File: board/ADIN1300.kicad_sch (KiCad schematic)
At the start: 38 parts, among them U1 ADIN1300BCPZ, U2 TLV71209_SOT23-5, Y1 Crystal_GND24_Small

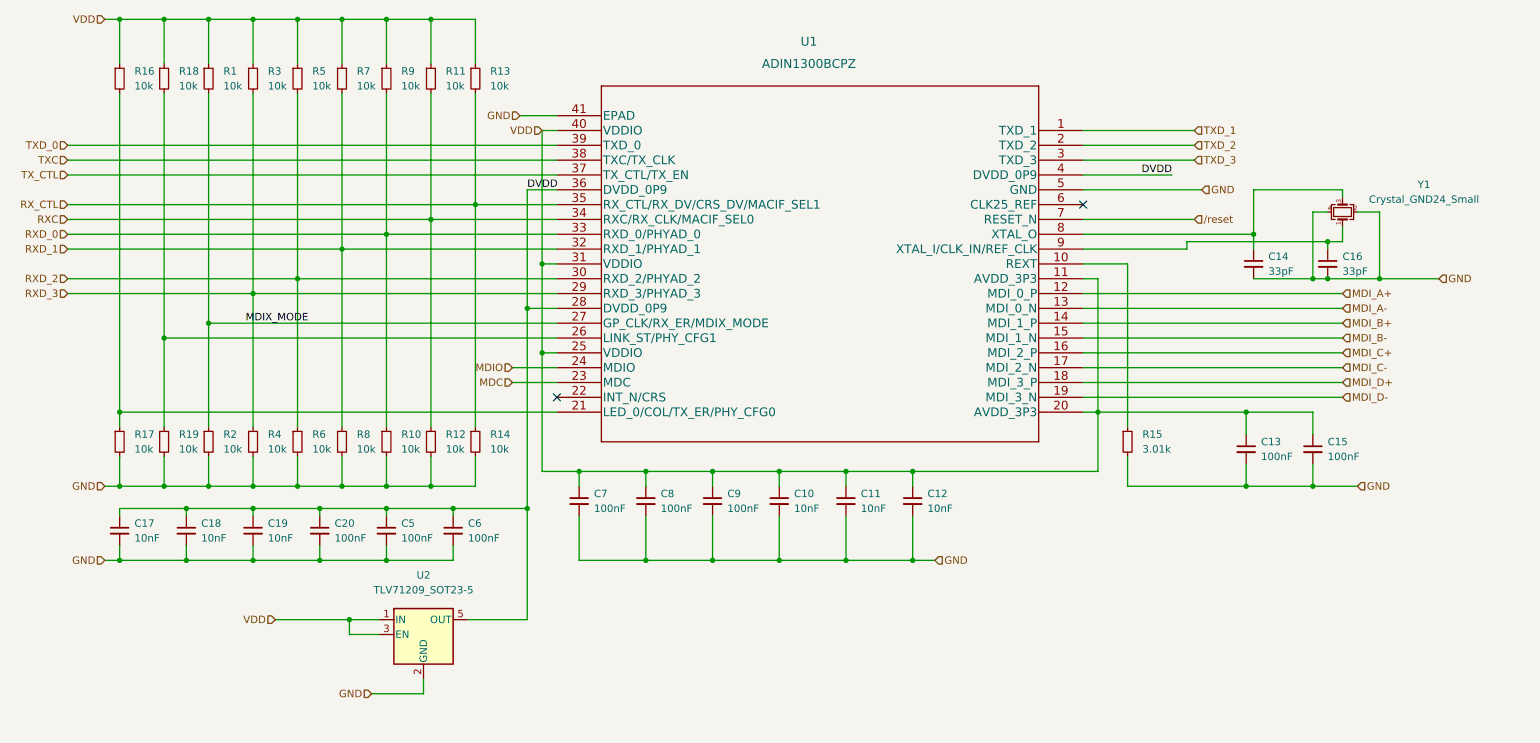
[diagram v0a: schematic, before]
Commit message: optimized EMI
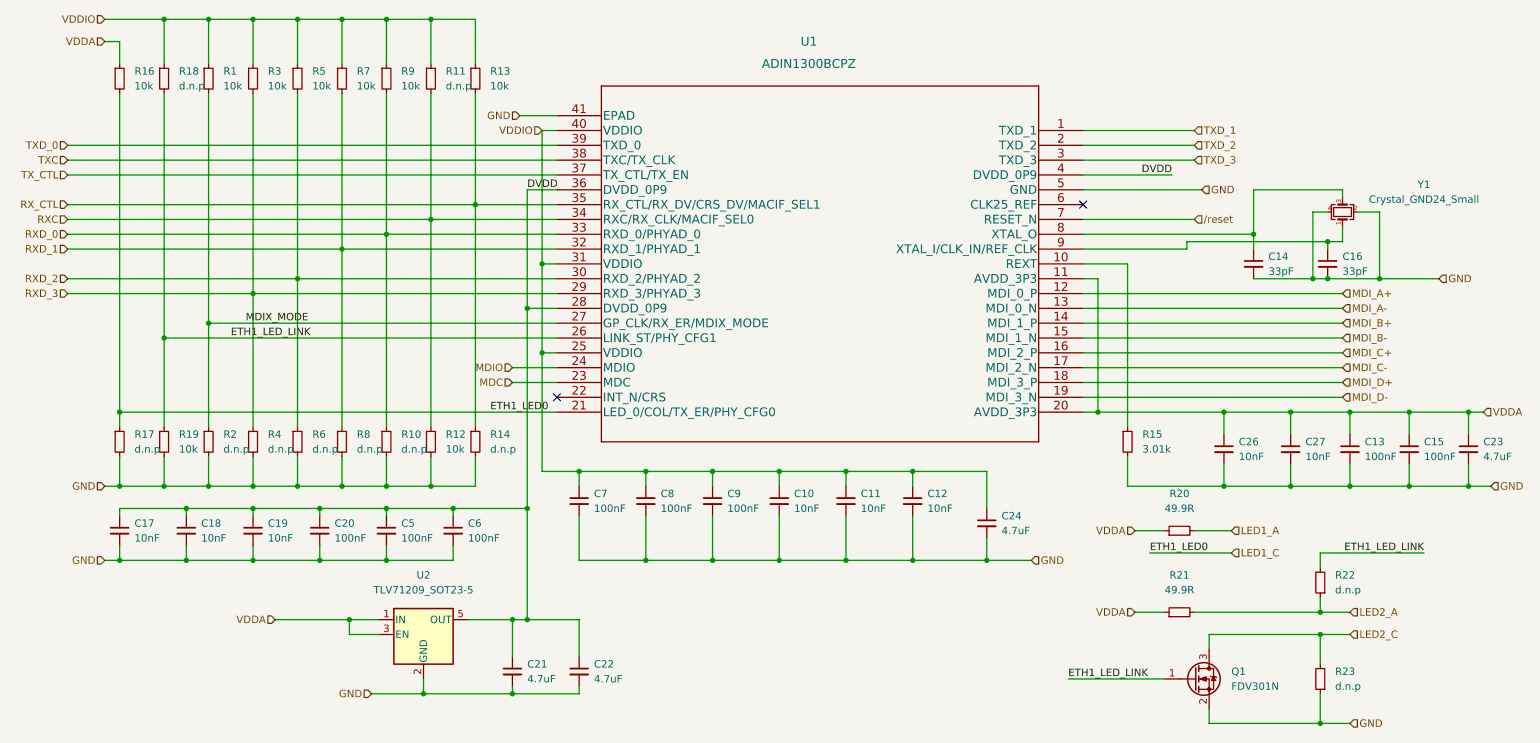
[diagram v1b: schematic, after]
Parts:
- added C21, C22, C23, C24: 4.7uF, Capacitor_SMD:C_0603_1608Metric, symbol Device:C_Small
- added C26, C27: 10nF, Capacitor_SMD:C_0603_1608Metric, symbol Device:C_Small
- added Q1: FDV301N, Package_TO_SOT_SMD:SOT-23, symbol Device:Q_NMOS_GSD
- added R20, R21: 49.9R, Resistor_SMD:R_0603_1608Metric, symbol Device:R_Small
- added R22, R23: d.n.p, Resistor_SMD:R_0603_1608Metric, symbol Device:R_Small
- R10, R11, R14, R17, R18, R2, R4, R6, R8: value 10k -> d.n.p
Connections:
- net DVDD: now also C21.1, C22.1
- net GND: now also C21.2, C22.2, C23.2, C24.2, C26.2, C27.2, Q1.2 (S), R23.1
- net LED1_C: now reaches R16.2, R17.1, U1.21 (LED_0/COL/TX_ER/PHY_CFG0)
- net ETH1_LED_LINK: now reaches R18.2, R19.1, U1.26 (LINK_ST/PHY_CFG1)
- net ETH1_LED_LINK: now also Q1.1 (G), R22.2
- net VDD renamed VDDIO
- net VDDIO: now also C24.1; no longer C13.1, C15.1, R16.1, U1.11 (AVDD_3P3), U1.20 (AVDD_3P3), U2.1 (IN), U2.3 (EN)
- new net LED1_A: R20.2
- new net LED2_A: R21.2, R22.1
- new net LED2_C: Q1.3 (D), R23.2
- new net VDDA: C13.1, C15.1, C23.1, C26.1, C27.1, R16.1, R20.1, R21.1, U1.11 (AVDD_3P3), U1.20 (AVDD_3P3), U2.1 (IN), U2.3 (EN)
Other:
- moved on the sheet: C13, C15

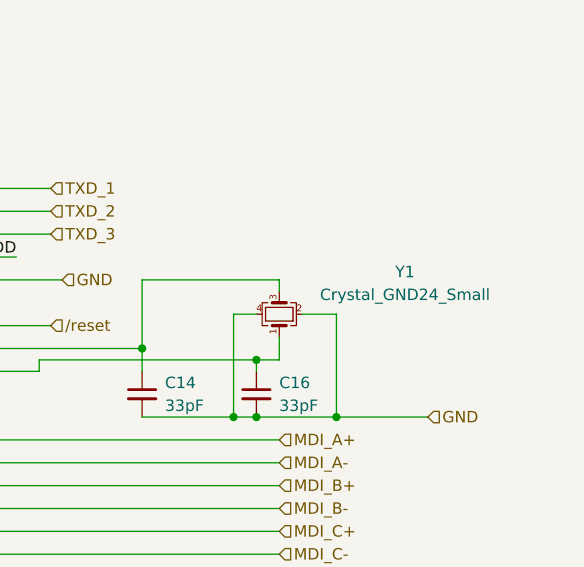
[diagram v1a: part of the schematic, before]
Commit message: specified crystal frequentcy
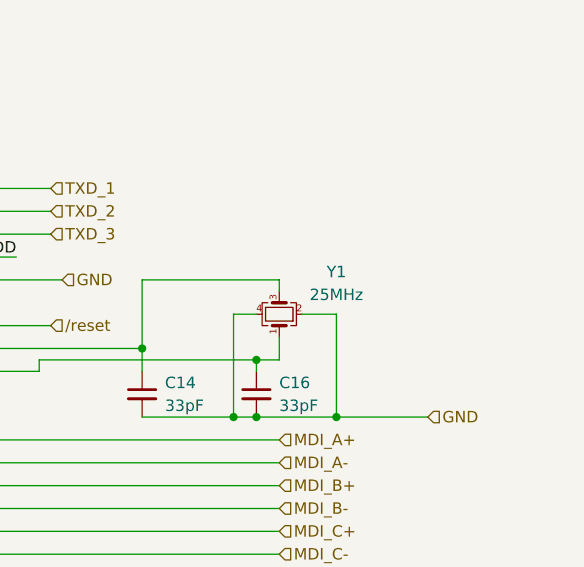
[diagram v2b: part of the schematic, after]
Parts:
- Y1: value Crystal_GND24_Small -> 25MHz
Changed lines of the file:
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@@
   (symbol (lib_id "Device:Crystal_GND24_Small") (at 252.73 76.2 90) (unit 1)
     (in_bom yes) (on_board yes) (fields_autoplaced)
-    (property "Reference" "Y1" (id 0) (at 266.7 71.501 90))
-    (property "Value" "Crystal_GND24_Small" (id 1) (at 266.7 74.041 90))
+    (property "Reference" "Y1" (id 0) (at 259.08 71.501 90))
+    (property "Value" "25MHz" (id 1) (at 259.08 74.041 90))
     (property "Footprint" "Crystal:Crystal_SMD_Abracon_ABM8G-4Pin_3.2x2.5mm" (id 2) (at 252.73 76.2 0)
       (effects (font (size 1.27 1.27)) hide)
